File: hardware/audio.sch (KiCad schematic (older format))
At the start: 62 parts, among them U12 TL074, U13 LM1972, U14 TPA3138D2, U15 74HCT4053

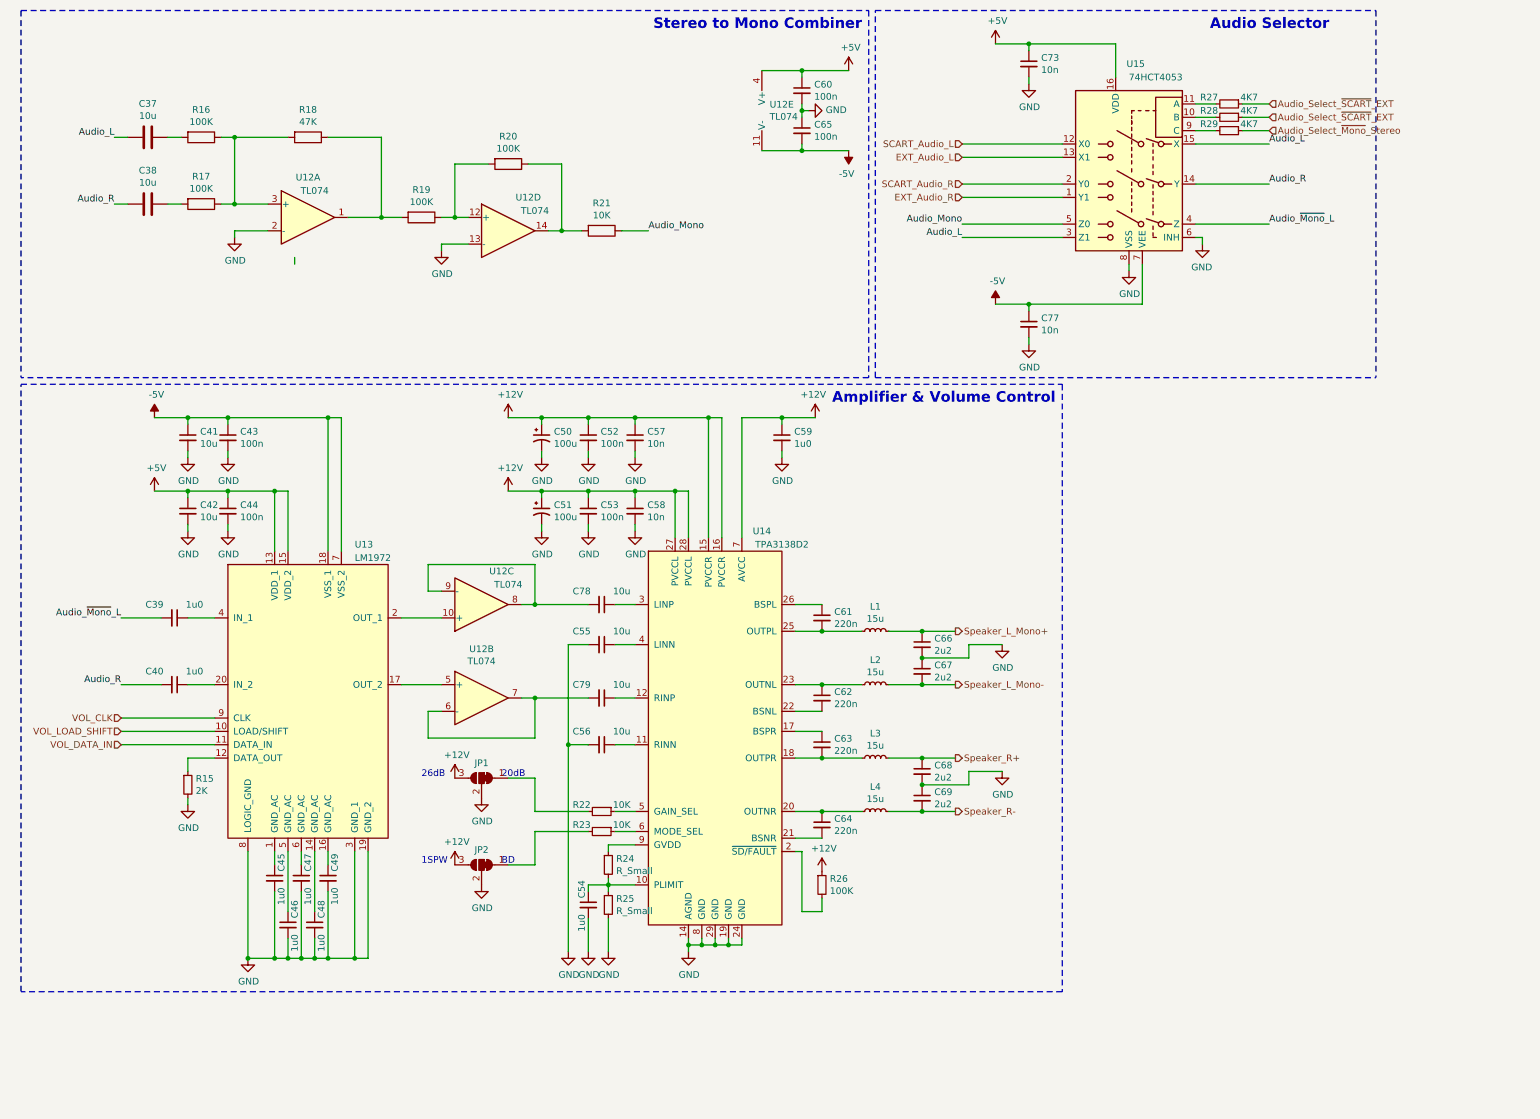
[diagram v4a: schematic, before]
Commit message: Started major rework on the Audio section (chose the wrong amplifier as it can't drive 4Ohm loads) Moved over to nightly Kicad v 5.9 versions. Was a mistake to do, but will look into reverting another time.
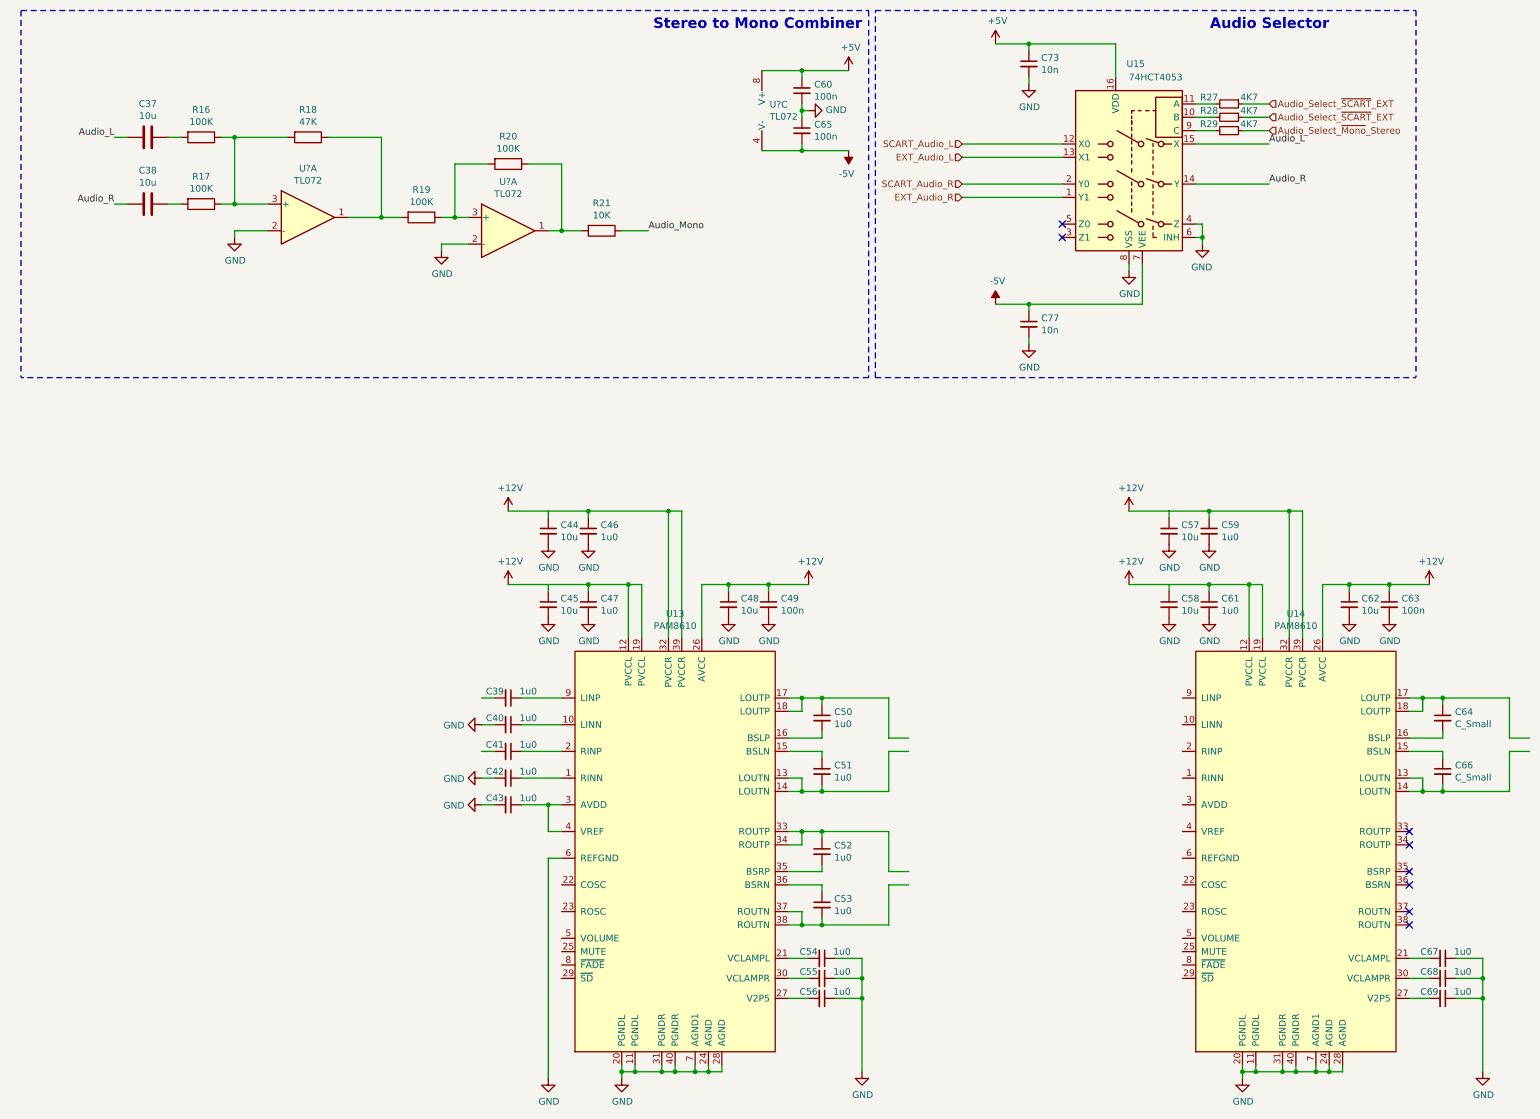
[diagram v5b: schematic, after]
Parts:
- removed C50, C51: 100u, Capacitor_SMD:CP_Elec_8x10.5, symbol Device:CP1_Small
- removed C78, C79: 10u, Capacitor_SMD:C_0805_2012Metric, symbol Device:C_Small
- removed JP1, JP2: SolderJumper_3_Bridged12, Jumper:SolderJumper-3_P1.3mm_Bridged12_Pad1.0x1.5mm, symbol Jumper:SolderJumper_3_Bridged12
- removed L1, L2, L3, L4: 15u, Inductor_SMD:L_10.4x10.4_H4.8, symbol Device:L_Small
- removed R15: 2K, Resistor_SMD:R_0603_1608Metric, symbol Device:R_Small
- removed R22, R23: 10K, Resistor_SMD:R_0603_1608Metric, symbol Device:R_Small
- removed R24, R25: R_Small, Resistor_SMD:R_0603_1608Metric, symbol Device:R_Small
- removed R26: 100K, Resistor_SMD:R_0603_1608Metric, symbol Device:R_Small
- removed U12: TL074, Package_SO:TSSOP-14_4.4x5mm_P0.65mm, symbol Amplifier_Operational:TL074
- removed U13: LM1972, Package_SO:SOIC-20W_7.5x12.8mm_P1.27mm, symbol Console2JAMMA:LM1972
- removed U14: TPA3138D2, Package_SO:TSSOP-28-1EP_4.4x9.7mm_P0.65mm, symbol Console2JAMMA:TPA3138D2
- added C50, C51: 1u0, Capacitor_SMD:C_0603_1608Metric, symbol Device:C_Small
- added U13, U14: PAM8610, Package_DFN_QFN:QFN-40-1EP_6x6mm_P0.5mm_EP4.6x4.6mm_ThermalVias, symbol Console2JAMMA:PAM8610
- added U? (x3): TL072, symbol Amplifier_Operational:TL072
- C39, C40: footprint Capacitor_SMD:C_0805_2012Metric -> Capacitor_SMD:C_0603_1608Metric
- C41, C42, C55, C56: value 10u -> 1u0; footprint Capacitor_SMD:C_0805_2012Metric -> Capacitor_SMD:C_0603_1608Metric
- C43, C52, C53: value 100n -> 1u0
- C44: value 100n -> 10u; footprint Capacitor_SMD:C_0603_1608Metric -> Capacitor_SMD:C_0805_2012Metric
- C45, C48: value 1u0 -> 10u; footprint Capacitor_SMD:C_0603_1608Metric -> Capacitor_SMD:C_0805_2012Metric
- C49: value 1u0 -> 100n
- C57, C58: value 10n -> 10u; footprint Capacitor_SMD:C_0603_1608Metric -> Capacitor_SMD:C_0805_2012Metric
- C61: value 220n -> 1u0; footprint Capacitor_SMD:C_1210_3225Metric -> Capacitor_SMD:C_0603_1608Metric
- C62: value 220n -> 10u; footprint Capacitor_SMD:C_1210_3225Metric -> Capacitor_SMD:C_0805_2012Metric
- C63: value 220n -> 100n; footprint Capacitor_SMD:C_1210_3225Metric -> Capacitor_SMD:C_0603_1608Metric
- C64: value 220n -> C_Small; footprint Capacitor_SMD:C_1210_3225Metric -> Capacitor_SMD:C_0603_1608Metric
- C66: value 2u2 -> C_Small; footprint Capacitor_SMD:C_1210_3225Metric -> Capacitor_SMD:C_0603_1608Metric
- C67, C68, C69: value 2u2 -> 1u0; footprint Capacitor_SMD:C_1210_3225Metric -> Capacitor_SMD:C_0603_1608Metric
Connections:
- net labels removed: Audio_~Mono~_L, Speaker_L_Mono+, Speaker_L_Mono-, Speaker_R+, Speaker_R-, VOL_CLK, VOL_DATA_IN, VOL_LOAD_SHIFT
- wire segments 224 -> 227
- no-connect marks 0 -> 8
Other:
- note removed: "1SPW"
- note removed: "20dB"
- note removed: "26dB"
- note removed: "Amplifier & Volume Control"
- note removed: "BD"
